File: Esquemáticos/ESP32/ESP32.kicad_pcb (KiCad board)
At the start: 2 copper layers, 66 parts, among them J1 Conector para bobinas del mot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, J2 Conector para bobinas del mot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, J3 Barrel_Jack, J4 USB Programador, Q1 S8550, Q2 S8550, Q3 S8550, Q4 S8550, Q5 S8550, Q6 S8550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

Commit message: wey noooooooooo (no guardé xd)
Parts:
- moved J4 190.0 mm to (325.0, 35.0)
- moved R22 184.1 mm to (347.3, 102.2)
- moved R4 184.1 mm to (350.2, 99.6)
- moved C2 184.1 mm to (347.3, 107.2)
- moved D1 184.1 mm to (292.8, 86.1)
- moved D2 184.1 mm to (311.3, 55.0)
- moved J1 184.1 mm to (338.7, 94.9)
- moved J2 184.1 mm to (384.2, 72.8)
- moved Q1 184.1 mm to (354.9, 86.2)
- moved Q2 184.1 mm to (347.2, 93.6)
- moved Q6 184.1 mm to (354.9, 81.7)
- moved R16 184.1 mm to (354.6, 99.6)
- moved R17 184.1 mm to (357.5, 92.2)
- moved R2 184.1 mm to (337.6, 108.6)
- moved R21 184.1 mm to (347.3, 104.7)
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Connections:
- C1 pad 1: +12V -> GND
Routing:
- net GND: track 0.00 -> 9.13 mm
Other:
- board outline added: 100 x 100 mm

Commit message: PCB versión 1 (Faltan zonas de GND)
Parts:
- J1, J2: footprint Connector_JST:JST_AUH_BM05B-AUHKS-GA-TB_1x05-1MP_P1.50mm_Vertical -> Connector_JST:JST_EH_B5B-EH-A_1x05_P2.50mm_Vertical
- moved Q4 223.8 mm to (139.7, 119.4), turned to -90 degrees
- moved R9 223.6 mm to (139.7, 124.5), turned to -90 degrees
- moved R10 216.9 mm to (147.3, 124.5), turned to -90 degrees
- moved C1 216.5 mm to (142.2, 137.2), turned to 90 degrees
- moved R7 215.7 mm to (149.9, 96.5), turned to -90 degrees
- moved R3 213.3 mm to (147.3, 114.3), turned to 180 degrees
- moved R4 211.0 mm to (139.7, 114.3), turned to 180 degrees
- moved J2 209.9 mm to (188.0, 147.3), turned to 180 degrees
- moved R8 209.7 mm to (144.8, 96.5), turned to -90 degrees
- moved SW1 208.6 mm to (104.1, 127.8), turned to 90 degrees
- moved Q3 206.9 mm to (147.3, 119.4), turned to -90 degrees
- moved R11 206.7 mm to (154.9, 124.5), turned to -90 degrees
- moved R12 205.2 mm to (162.6, 124.5), turned to -90 degrees
- moved R1 202.2 mm to (162.6, 114.3)
- moved U3 201.7 mm to (152.4, 137.2), turned to -90 degrees
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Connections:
- net Net-(R28-Pad1) renamed /Principal/HelloWorld
- net Net-(RRX1-Pad1) renamed /Principal/RX
- net Net-(RTX1-Pad1) renamed /Principal/TX
- C1 pad 1: GND -> +12V
- J1 pad 1: Net-(J1-Pad1) -> +12V
- J1 pad 5: (no net) -> Net-(J1-Pad5)
- J2 pad 1: Net-(J2-Pad1) -> +12V
- J2 pad 5: (no net) -> Net-(J2-Pad5)
- U3 pad 13: Net-(J1-Pad4) -> Net-(J1-Pad5)
- U3 pad 14: Net-(J1-Pad3) -> Net-(J1-Pad4)
- U3 pad 15: Net-(J1-Pad2) -> Net-(J1-Pad3)
- U3 pad 16: Net-(J1-Pad1) -> Net-(J1-Pad2)
- U4 pad 13: Net-(J2-Pad4) -> Net-(J2-Pad5)
- U4 pad 14: Net-(J2-Pad3) -> Net-(J2-Pad4)
- U4 pad 15: Net-(J2-Pad2) -> Net-(J2-Pad3)
- U4 pad 16: Net-(J2-Pad1) -> Net-(J2-Pad2)
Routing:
- net GND: track 9.13 -> 499.0 mm, vias 0 -> 9
- net +5V: track 0.00 -> 215.7 mm, vias 0 -> 2
- net +3.3V: track 0.00 -> 184.8 mm
- net +12V: track 0.00 -> 156.7 mm
- net /Motores/GNDL: track 0.00 -> 47.3 mm
- net /Principal/RST: track 0.00 -> 42.6 mm, vias 0 -> 1
- net /Principal/SS: track 0.00 -> 40.6 mm, vias 0 -> 1
- net /Principal/TX: track 0.00 -> 39.3 mm, vias 0 -> 2
- net /Principal/SCK: track 0.00 -> 39.2 mm, vias 0 -> 1
- net /Principal/MOSI: track 0.00 -> 36.7 mm
- net /Principal/MISO: track 0.00 -> 35.3 mm
- net /Principal/EN/RST: track 0.00 -> 34.6 mm, vias 0 -> 2
- net /Principal/RX: track 0.00 -> 33.5 mm, vias 0 -> 2
- net /Motores/Out1: track 0.00 -> 25.9 mm, vias 0 -> 3
- net /Motores/Out8: track 0.00 -> 25.3 mm, vias 0 -> 2
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
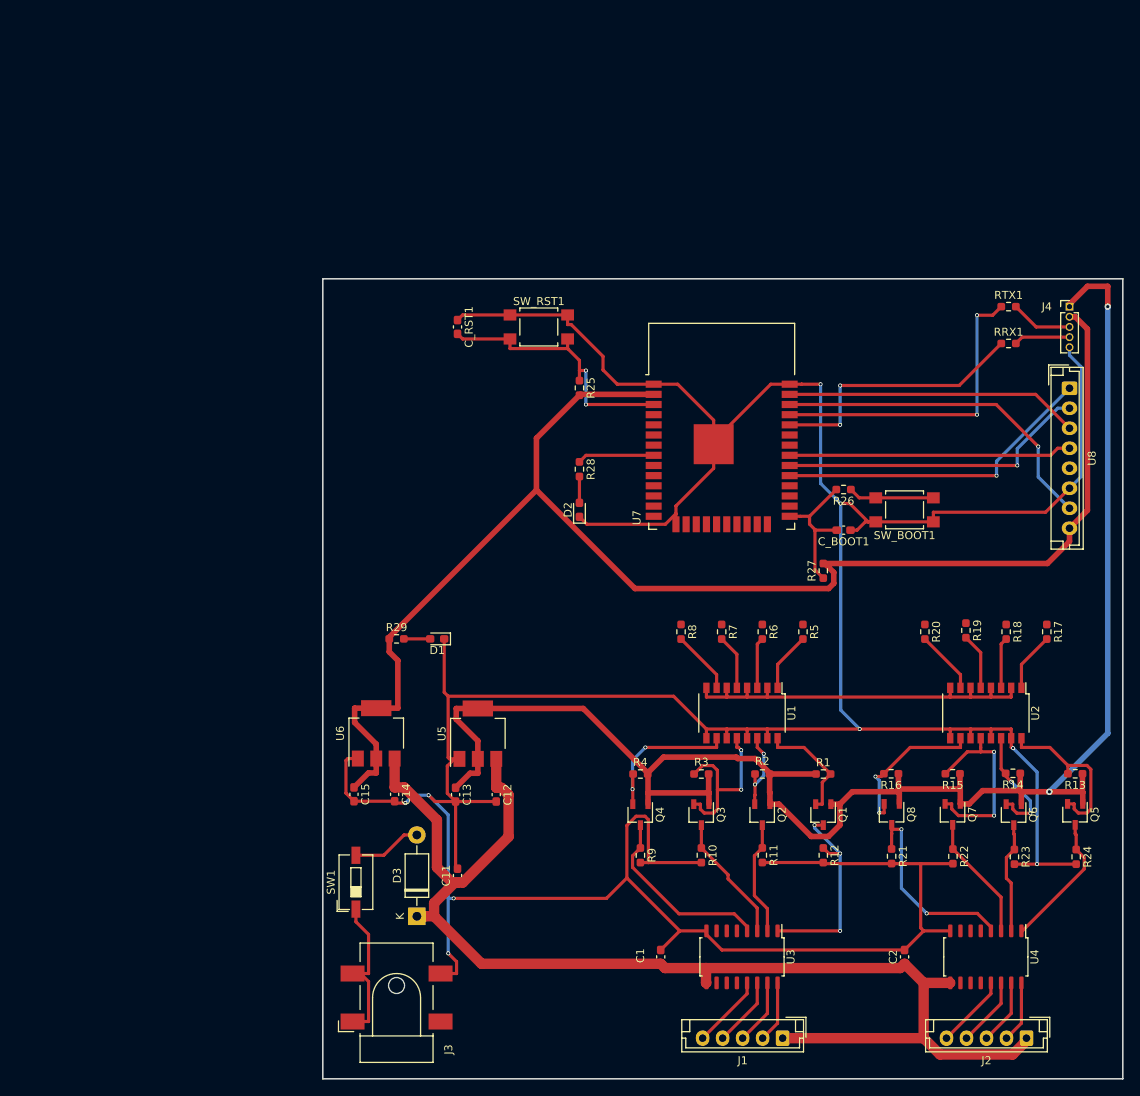
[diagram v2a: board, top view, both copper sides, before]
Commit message: Ruteo y zonas de cobre. Modo_serio.jpg
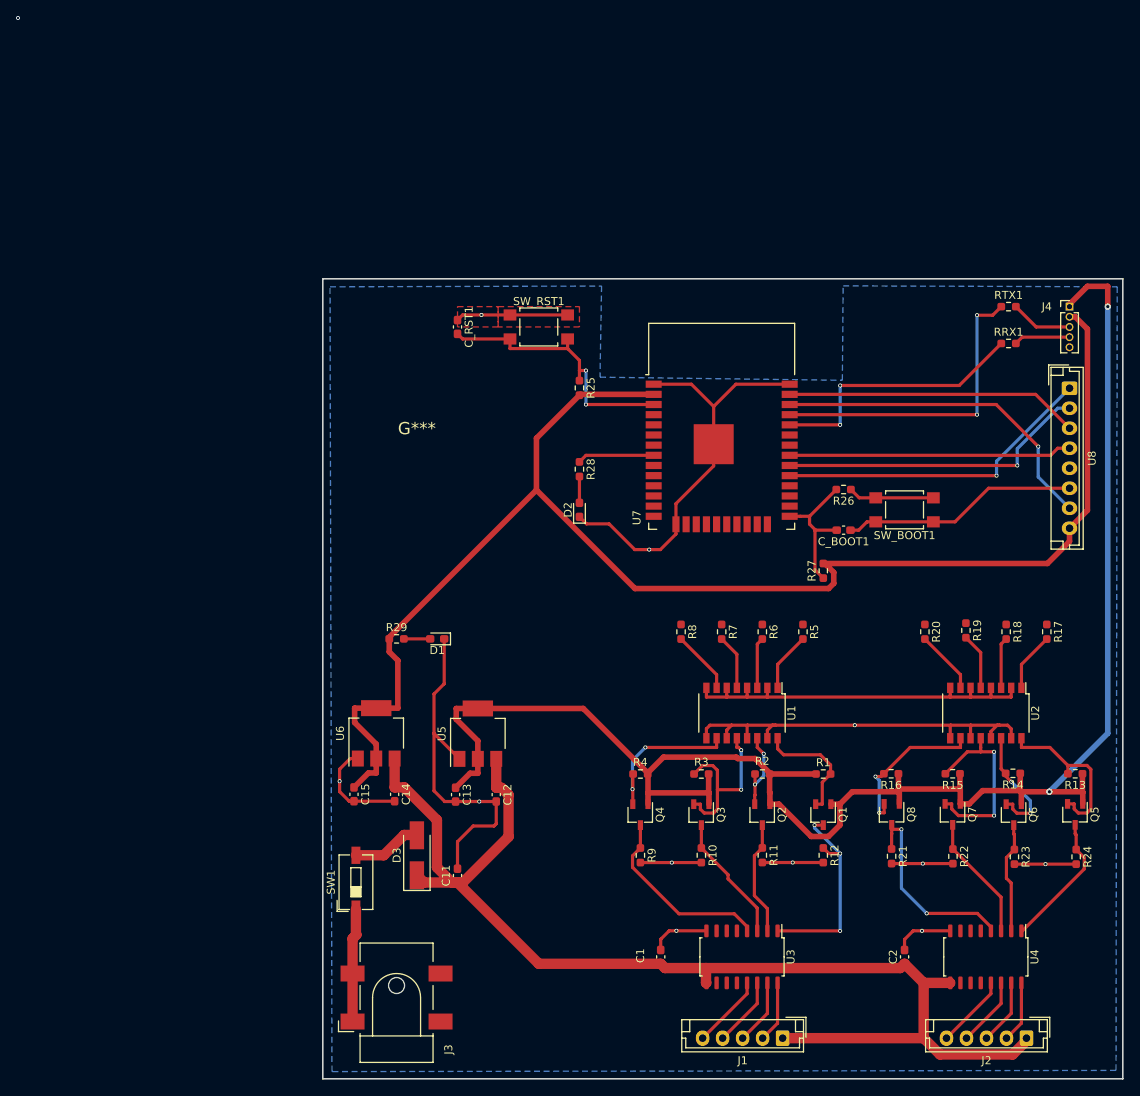
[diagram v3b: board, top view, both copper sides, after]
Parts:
- added G***: LOGO, Libraryxd:SMRW, F.Cu at (111.8, 71.1)
- C14: value 22u -> 10uF
- C15: value 22u -> 22uF
- D3: footprint Diode_THT:D_DO-41_SOD81_P10.16mm_Horizontal -> Diode_SMD:D_SMA_Handsoldering
- moved D3 7.62 mm to (111.8, 124.5)
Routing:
- net GND: track 499.0 -> 250.5 mm, vias 9 -> 11
- net Net-(J3-Pad1): track 19.1 -> 14.3 mm
- net +12V: track 156.7 -> 153.2 mm
- net Net-(Q1-Pad2): track 14.2 -> 14.9 mm
- net (no net): vias 0 -> 1
- added copper zone on B.Cu, net GND
- added copper zone on F.Cu, net GND

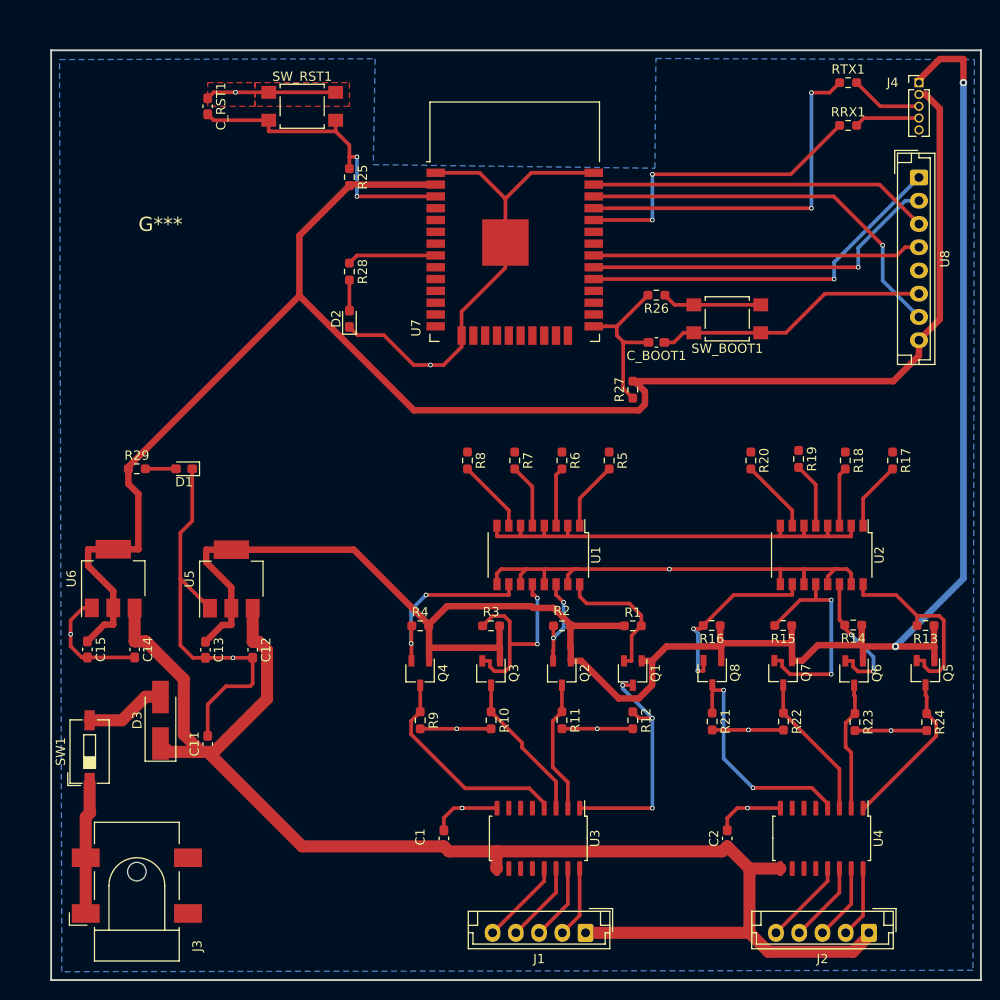
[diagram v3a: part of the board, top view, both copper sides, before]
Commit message: Muchos cambios a la PCB
Moví varios elementos para poder añadir los agujeros de montaje y agregué esos agujeros de montaje.

También moví el pulsador de BOOT para que quede estéticamente mejor a ambos lados del módulo ESP32 WROOM

Importante:
Nos faltan todas las conexiones de los optoacopladores con la ESP 32 xD (urgente revisar cuales pines sirven para eso).
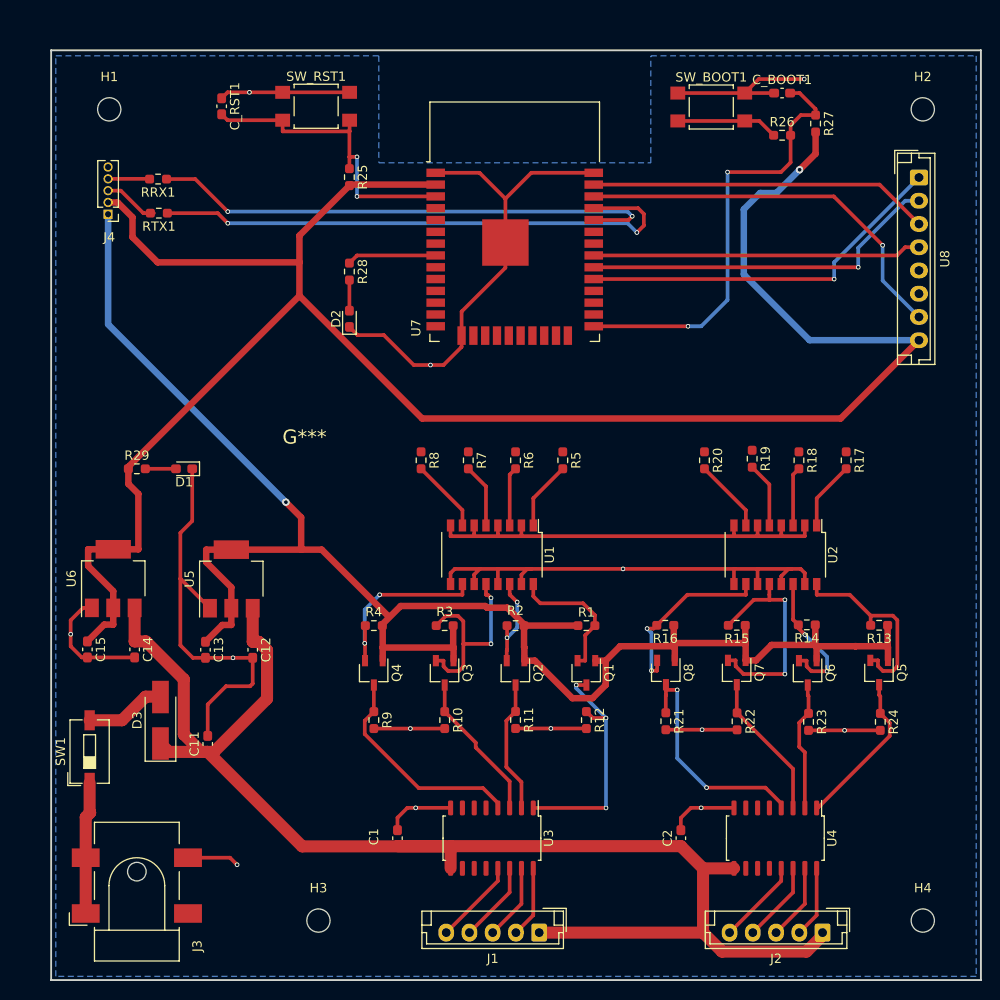
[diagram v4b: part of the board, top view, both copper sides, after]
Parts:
- added H1: MountingHole, MountingHole:MountingHole_2.5mm, F.Cu at (106.2, 58.8)
- added H2: MountingHole, MountingHole:MountingHole_2.5mm, F.Cu at (193.8, 58.8)
- added H3: MountingHole, MountingHole:MountingHole_2.5mm, F.Cu at (128.8, 146.0)
- added H4: MountingHole, MountingHole:MountingHole_2.5mm, F.Cu at (193.8, 146.0)
- moved J4 88.4 mm to (106.1, 70.0), turned to 180 degrees
- moved RTX1 75.4 mm to (111.6, 69.9), turned to 180 degrees
- moved RRX1 74.4 mm to (111.5, 66.2), turned to 180 degrees
- moved R27 34.7 mm to (182.2, 60.3), turned to -90 degrees
- moved C_BOOT1 30.0 mm to (178.6, 57.0), turned to 0 degrees
- moved G*** 27.6 mm to (127.2, 94.0)
- moved SW_BOOT1 22.8 mm to (171.0, 58.5), turned to 0 degrees
- moved R26 21.9 mm to (178.6, 61.5), turned to 0 degrees
- moved C1 4.99 mm to (137.2, 137.1)
- moved C2 4.99 mm to (167.7, 137.1)
- moved J2 4.99 mm to (183.0, 147.3)
- moved Q1 4.99 mm to (157.6, 119.4)
- moved Q2 4.99 mm to (149.9, 119.4)
- moved Q5 4.99 mm to (189.1, 119.3)
- moved Q6 4.99 mm to (181.4, 119.4)
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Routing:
- net +3.3V: track 184.8 -> 218.3 mm, vias 0 -> 1
- net +5V: track 215.7 -> 183.4 mm, vias 2 -> 1
- net /Principal/BOOT: track 18.4 -> 47.8 mm, vias 0 -> 2
- net /Principal/RX: track 33.5 -> 56.1 mm
- net /Principal/TX: track 39.3 -> 59.3 mm
- net GND: track 250.5 -> 243.9 mm, vias 11 -> 13
- net Net-(J4-Pad4): track 7.04 -> 4.01 mm
- net Net-(J4-Pad3): track 7.76 -> 5.93 mm
- net /Principal/EN/RST: track 34.6 -> 34.0 mm
- removed copper zone on F.Cu, net GND

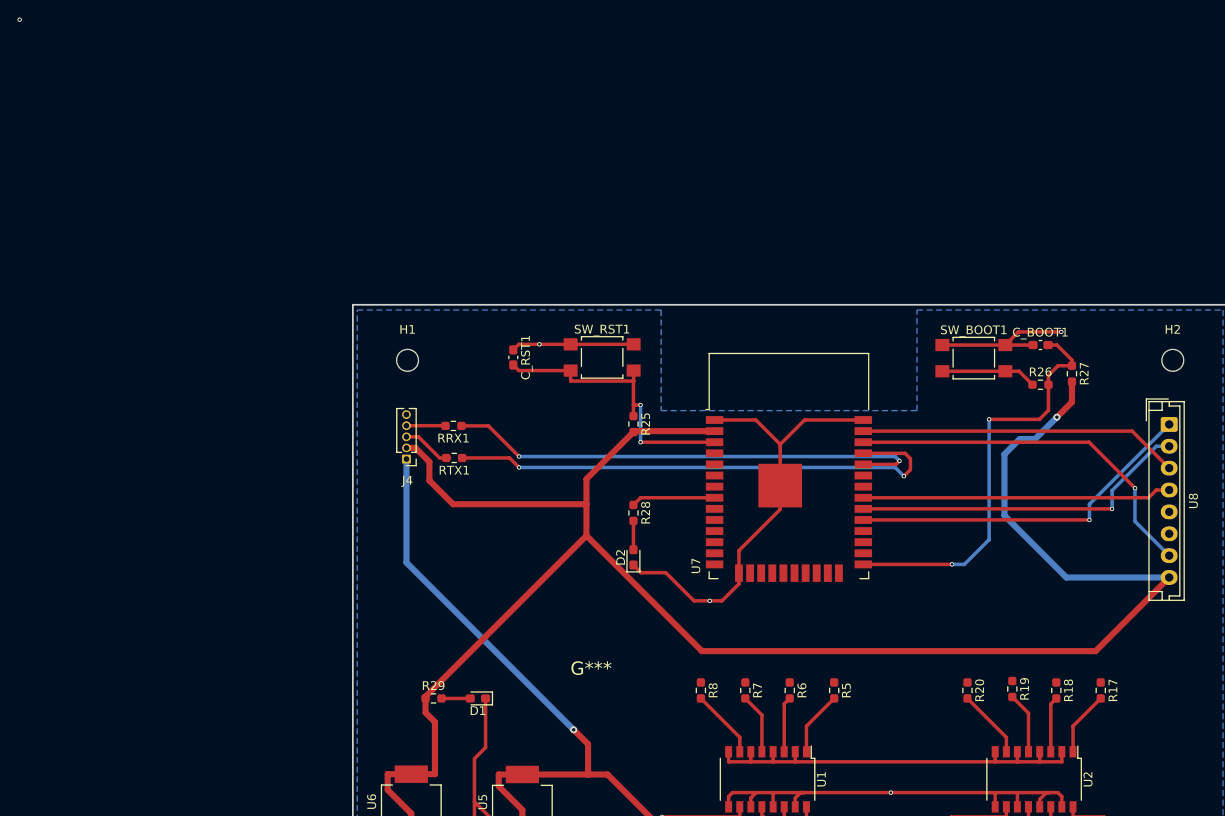
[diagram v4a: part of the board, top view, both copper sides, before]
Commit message: Añadí las conexiones con los optoacopladores
Además arreglé la posición de algunas vías.
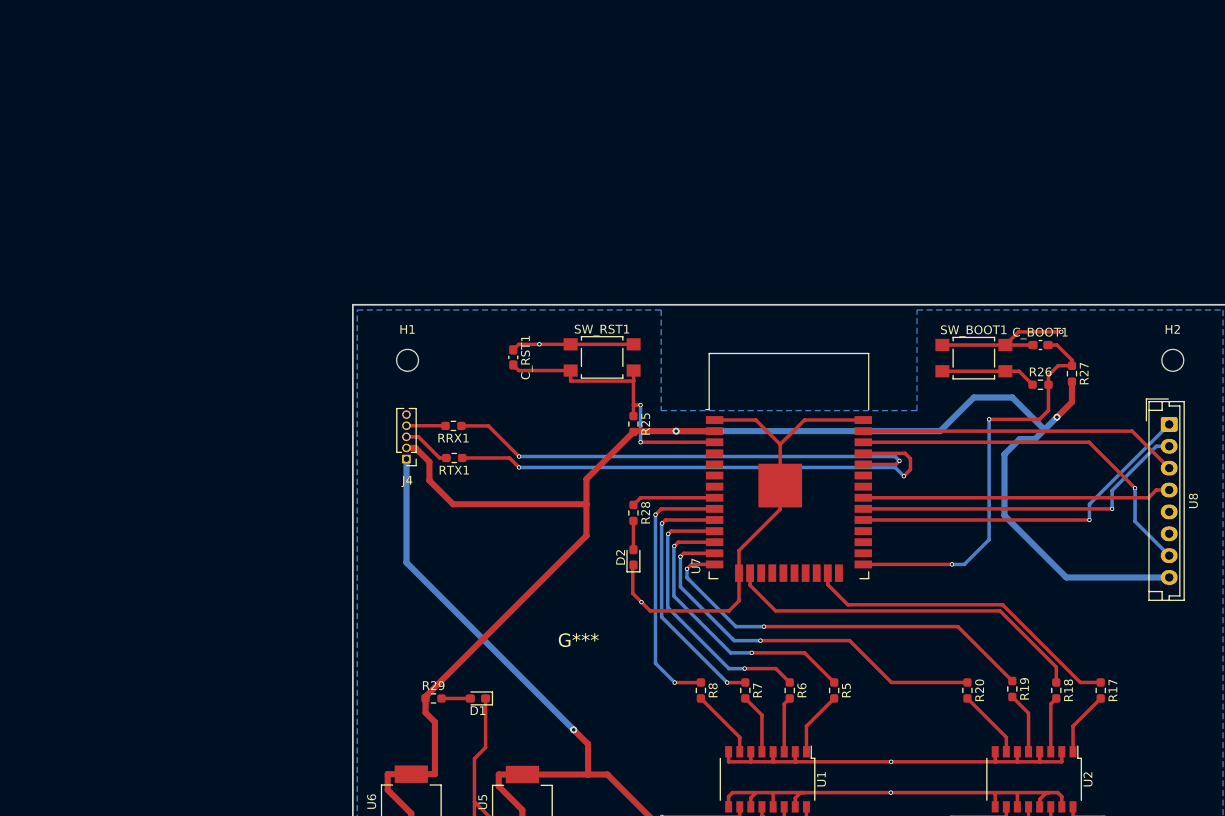
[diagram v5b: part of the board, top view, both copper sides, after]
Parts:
- moved G*** 3.51 mm to (125.8, 90.8)
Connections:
- U1 pad 2: /Motores/GNDL -> GND
- U1 pad 4: /Motores/GNDL -> GND
- U1 pad 6: /Motores/GNDL -> GND
- U1 pad 8: /Motores/GNDL -> GND
- U2 pad 2: /Motores/GNDL -> GND
- U2 pad 4: /Motores/GNDL -> GND
- U2 pad 6: /Motores/GNDL -> GND
- U2 pad 8: /Motores/GNDL -> GND
- U7 pad 10: unconnected-(U7-Pad10) -> /Motores/In3
- U7 pad 11: unconnected-(U7-Pad11) -> /Motores/In2
- U7 pad 12: unconnected-(U7-Pad12) -> /Motores/In1
- U7 pad 13: unconnected-(U7-Pad13) -> /Motores/In8
- U7 pad 14: unconnected-(U7-Pad14) -> /Motores/In7
- U7 pad 16: unconnected-(U7-Pad16) -> /Motores/In6
- U7 pad 23: unconnected-(U7-Pad23) -> /Motores/In5
- U7 pad 9: unconnected-(U7-Pad9) -> /Motores/In4
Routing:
- net GND: track 243.9 -> 295.3 mm, vias 13 -> 14
- net /Motores/GNDL: track 47.3 -> 0.00 mm
- net /Motores/In7: track 0.00 -> 46.5 mm, vias 0 -> 2
- net /Motores/In8: track 0.00 -> 44.9 mm, vias 0 -> 2
- net /Motores/In6: track 0.00 -> 42.0 mm
- net /Motores/In5: track 0.00 -> 37.2 mm
- net /Motores/In1: track 0.00 -> 32.9 mm, vias 0 -> 2
- net /Motores/In2: track 0.00 -> 31.4 mm, vias 0 -> 2
- net +3.3V: track 218.3 -> 187.9 mm, vias 1 -> 2
- net /Motores/In4: track 0.00 -> 30.1 mm, vias 0 -> 2
- net /Motores/In3: track 0.00 -> 29.6 mm, vias 0 -> 2
- net (no net): vias 1 -> 0

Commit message: PCB terminada (pendiente de aprobación)
:sunglasses: :sunglasses: :sunglasses:
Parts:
- J4: footprint Connector_PinHeader_1.27mm:PinHeader_1x05_P1.27mm_Vertical -> Connector_PinHeader_2.54mm:PinHeader_1x05_P2.54mm_Vertical
- moved J4 4.48 mm to (106.1, 74.5)
- moved RRX1 0.70 mm to (111.6, 67.0)
- moved RTX1 0.06 mm to (111.5, 69.9)
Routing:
- net GND: track 295.3 -> 0.00 mm, vias 14 -> 17
- net +5V: track 183.4 -> 178.9 mm
- net +3.3V: track 187.9 -> 184.4 mm
- net Net-(J4-Pad3): track 5.93 -> 4.71 mm
- net Net-(J4-Pad4): track 4.01 -> 4.58 mm
- added copper zone on F.Cu, net GND
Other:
- board text added: "PCB Smash Rows"
